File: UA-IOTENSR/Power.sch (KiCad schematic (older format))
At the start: 29 parts, among them IC1 BQ2000TPN-B5, J2 ZX62-AB-5PA_31_, U2 AP63203WU

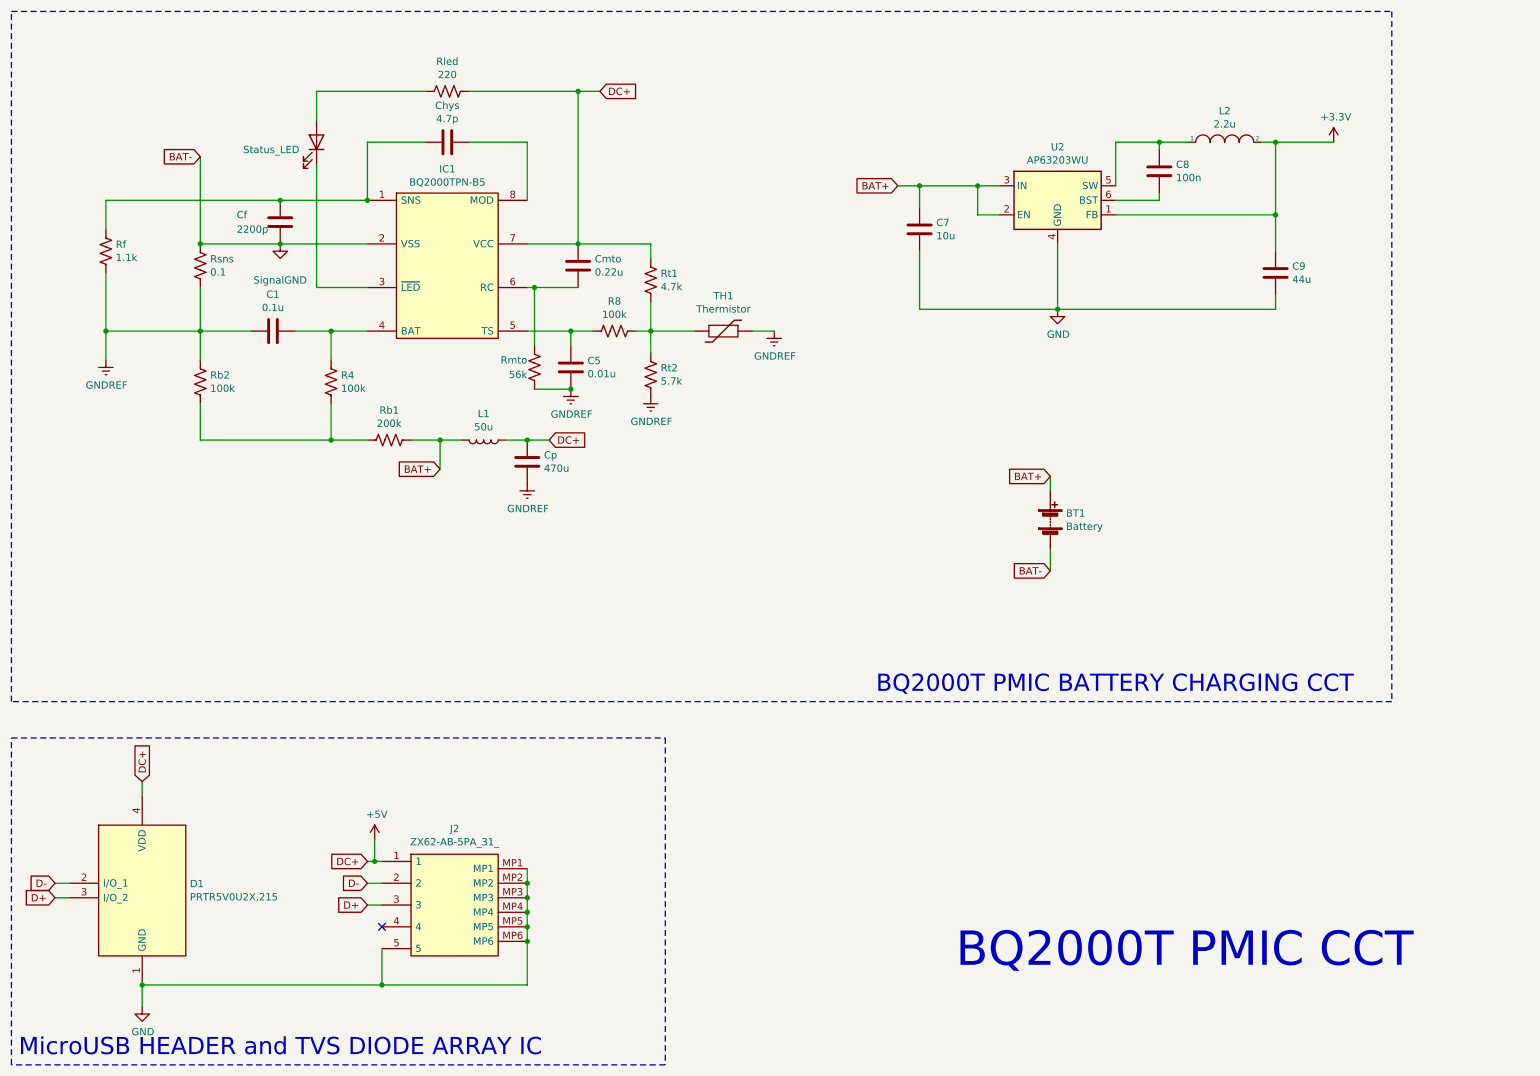
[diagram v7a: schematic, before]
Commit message: Fixed GNDs and added new capacitors
Adjusted ground connections, USB GND only connects to the Rf and the VCC by passing capacitors.
Added by pass capactitors on VCC.
Reconnected the thermistor in a pull high configuration
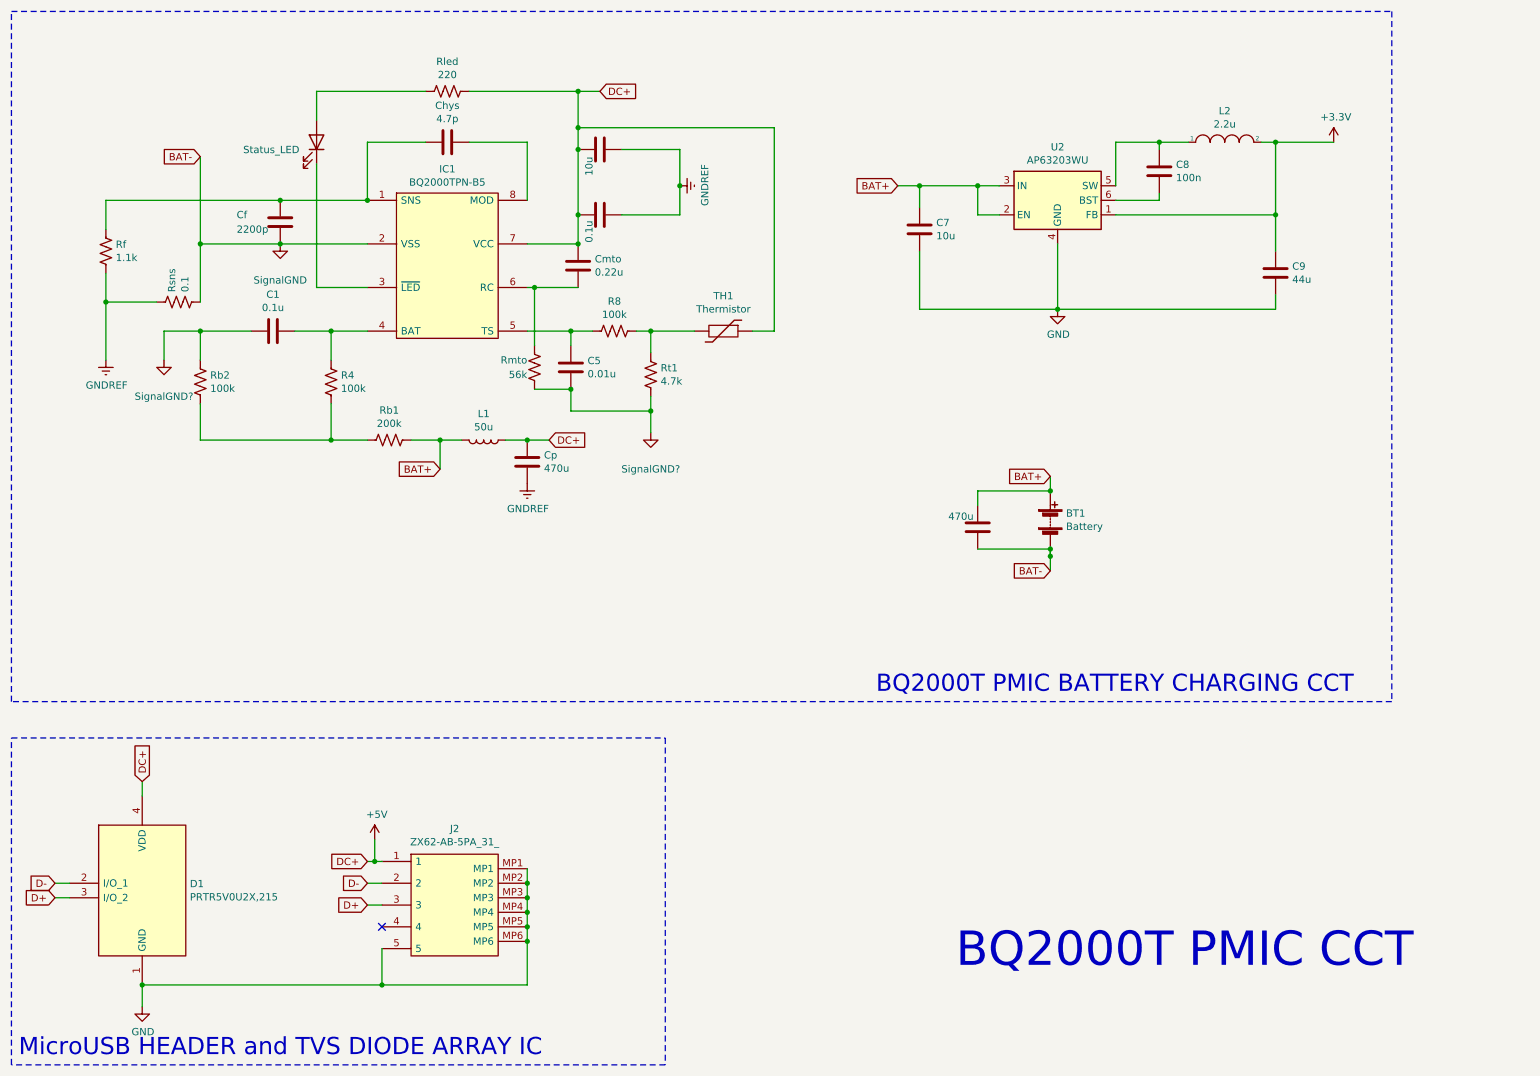
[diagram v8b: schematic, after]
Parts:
- removed Rt2: 5.7k, Resistor_SMD:R_0805_2012Metric_Pad1.20x1.40mm_HandSolder, symbol Device:R_US
- added Bypass_1: 10u, Capacitor_SMD:C_0805_2012Metric, symbol Device:C
- added Bypass_?: 0.1u, Capacitor_SMD:C_0805_2012Metric, symbol Device:C
- added Bypass_?: 470u, Capacitor_SMD:C_0805_2012Metric, symbol Device:C
- added SignalGND? (x2): GND, symbol power:GND
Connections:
- net +5V: now also TH1.1, Bypass_1.2, Bypass_?.2; no longer Rt1.1
- net BAT+: now also Bypass_?.2
- net GND: now also C1.2, C5.2, Rb2.1, Rmto.1, Rsns.2, Rt1.2, Bypass_?.1, SignalGND?.1 (GND), SignalGND?.1 (GND); no longer Rsns.1
- net GNDREF: now also Rsns.1, Bypass_1.1, Bypass_?.1; no longer C1.2, C5.2, Rb2.1, Rmto.1, Rsns.2, TH1.1
- net at R8.1, TH1.2: now also Rt1.1; no longer Rt1.2
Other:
- moved on the sheet: Rsns, Rt1
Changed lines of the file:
@@
 	0    1    1    0
 $EndComp
-Connection ~ 1150 2700
 $Comp
 L power:GNDREF #PWR07
@@
 L Device:R_US Rsns
 U 1 1 61E54493
-P 1800 2250
-F 0 "Rsns" H 1868 2296 50  0000 L CNN
-F 1 "0.1" H 1868 2205 50  0000 L CNN
-F 2 "SamacSys_Parts:RESC6331X80N" V 1840 2240 50  0001 C CNN
-F 3 "~" H 1800 2250 50  0001 C CNN
-	1    1800 2250
-	1    0    0    -1
-$EndComp
-Connection ~ 1800 2100
+P 1650 2500
+F 0 "Rsns" H 1718 2546 50  0000 L CNN
+F 1 "0.1" H 1718 2455 50  0000 L CNN
+F 2 "SamacSys_Parts:RESC6331X80N" V 1690 2490 50  0001 C CNN
+F 3 "~" H 1650 2500 50  0001 C CNN
+	1    1650 2500
+	0    -1   -1   0
+$EndComp
 $Comp
 L Device:C Cf
@@
 	1    0    0    -1
 $EndComp
-Wire Wire Line
-	1150 2700 1150 2900
 $Comp
 L Device:R_US Rb2
@@
 	3650 1050 4400 1050
 Wire Wire Line
-	4400 1050 4400 2100
-Wire Wire Line
 	3250 3450 3450 3450
 $Comp
@@
 Connection ~ 4900 2700
 $Comp
-L power:GNDREF #PWR013
-U 1 1 61E7A638
-P 4900 3150
-F 0 "#PWR013" H 4900 2900 50  0001 C CNN
-F 1 "GNDREF" H 4905 2977 50  0000 C CNN
-F 2 "" H 4900 3150 50  0001 C CNN
-F 3 "" H 4900 3150 50  0001 C CNN
-	1    4900 3150
-	1    0    0    -1
-$EndComp
-$Comp
 L Device:Thermistor TH1
 U 1 1 61E7B984
@@
 Wire Wire Line
 	4900 2700 5200 2700
-$Comp
-L power:GNDREF #PWR014
-U 1 1 61E7DEA9
-P 5750 2700
-F 0 "#PWR014" H 5750 2450 50  0001 C CNN
-F 1 "GNDREF" H 5755 2527 50  0000 C CNN
-F 2 "" H 5750 2700 50  0001 C CNN
-F 3 "" H 5750 2700 50  0001 C CNN
-	1    5750 2700
-	1    0    0    -1
-$EndComp
 Text GLabel 4200 3450 2    50   Input ~ 0
 DC+
@@
 Wire Wire Line
 	4350 3100 4100 3100
-$Comp
-L power:GNDREF #PWR012
-U 1 1 61E8BC9F
-P 4350 3100
-F 0 "#PWR012" H 4350 2850 50  0001 C CNN
-F 1 "GNDREF" H 4355 2927 50  0000 C CNN
-F 2 "" H 4350 3100 50  0001 C CNN
-F 3 "" H 4350 3100 50  0001 C CNN
-	1    4350 3100
-	1    0    0    -1
-$EndComp
-Connection ~ 4350 3100
 Wire Wire Line
 	4050 1800 4050 1400
@@
 	2950 1400 3350 1400
 Wire Wire Line
-	1150 2300 1150 2700
-Wire Wire Line
-	1800 2700 1150 2700
-Wire Wire Line
 	2150 2700 1800 2700
-Connection ~ 1800 2700
 Wire Wire Line
 	1800 2700 1800 2900
-Wire Wire Line
-	1800 2400 1800 2700
 Wire Wire Line
 	4050 2400 4100 2400
@@
 DC+
 NoConn ~ 3050 6800
-Wire Wire Line
-	4900 2100 4400 2100
-Wire Wire Line
-	4900 2200 4900 2100
-$Comp
-L Device:R_US Rt2
-U 1 1 6209F5C7
+$Comp
+L Device:R_US Rt1
+U 1 1 620A85C3
 P 4900 3000
-F 0 "Rt2" H 4968 3046 50  0000 L CNN
-F 1 "5.7k" H 4968 2955 50  0000 L CNN
+F 0 "Rt1" H 4968 3046 50  0000 L CNN
+F 1 "4.7k" H 4968 2955 50  0000 L CNN
 F 2 "Resistor_SMD:R_0805_2012Metric_Pad1.20x1.40mm_HandSolder" V 4940 2990 50  0001 C CNN
 F 3 "~" H 4900 3000 50  0001 C CNN
@@
 	1    0    0    -1
 $EndComp
-$Comp
-L Device:R_US Rt1
-U 1 1 620A85C3
-P 4900 2350
-F 0 "Rt1" H 4968 2396 50  0000 L CNN
-F 1 "4.7k" H 4968 2305 50  0000 L CNN
-F 2 "Resistor_SMD:R_0805_2012Metric_Pad1.20x1.40mm_HandSolder" V 4940 2340 50  0001 C CNN
-F 3 "~" H 4900 2350 50  0001 C CNN
-	1    4900 2350
-	1    0    0    -1
-$EndComp
-Wire Wire Line
-	4900 2500 4900 2700
 $Comp
 L Regulator_Switching:AP63203WU U2
@@
 	7650 3800 7650 3700
 Wire Wire Line
-	7650 4200 7650 4350
+	7650 4200 7650 4250
 Text GLabel 7650 3700 0    50   Input ~ 0
 BAT+
 Text GLabel 7650 4350 0    50   Input ~ 0
 BAT-
+Wire Wire Line
+	1150 2300 1150 2500
+Connection ~ 1150 2500
+Wire Wire Line
+	1150 2500 1150 2900
+Wire Wire Line
+	1800 2500 1800 2100
+Connection ~ 1800 2100
+Wire Wire Line
+	1150 2500 1500 2500
+$Comp
+L power:GND SignalGND?
+U 1 1 624B40F1
+P 1550 2900
+F 0 "SignalGND?" H 1550 2650 50  0000 C CNN
+F 1 "GND" H 1555 2727 50  0001 C CNN
+F 2 "" H 1550 2900 50  0001 C CNN
+F 3 "" H 1550 2900 50  0001 C CNN
+	1    1550 2900
+	1    0    0    -1
+$EndComp
+Connection ~ 1800 2700
+Wire Wire Line
+	1550 2700 1800 2700
+Wire Wire Line
+	1550 2700 1550 2900
+Wire Wire Line
+	5750 2700 5750 1300
+Wire Wire Line
+	5750 1300 4400 1300
+Wire Wire Line
+	4400 1050 4400 1300
+Connection ~ 4400 1300
+Wire Wire Line
+	4400 1300 4400 1450
+$Comp
+L power:GND SignalGND?
+U 1 1 624C105D
+P 4900 3400
+F 0 "SignalGND?" H 4900 3150 50  0000 C CNN
+F 1 "GND" H 4905 3227 50  0001 C CNN
+F 2 "" H 4900 3400 50  0001 C CNN
+F 3 "" H 4900 3400 50  0001 C CNN
+	1    4900 3400
+	1    0    0    -1
+$EndComp
+Wire Wire Line
+	4350 3100 4350 3250
+Wire Wire Line
+	4350 3250 4900 3250
+Wire Wire Line
+	4900 3150 4900 3250
+Connection ~ 4350 3100
+Connection ~ 4900 3250
+Wire Wire Line
+	4900 3250 4900 3400
+$Comp
+L Device:C Bypass_1
+U 1 1 624CCAA1
+P 4550 1450
+F 0 "Bypass_1" H 4665 1496 50  0001 C BNN
+F 1 "10u" H 4665 1405 50  0000 C TNN
+F 2 "Capacitor_SMD:C_0805_2012Metric" H 4588 1300 50  0001 C CNN
+F 3 "~" H 4550 1450 50  0001 C CNN
+	1    4550 1450
+	0    1    1    0
+$EndComp
+Connection ~ 4400 1450
+Wire Wire Line
+	4400 1450 4400 1900
+$Comp
+L Device:C Bypass_?
+U 1 1 624D22AD
+P 4550 1900
+F 0 "Bypass_?" H 4665 1946 50  0001 C BNN
+F 1 "0.1u" H 4665 1855 50  0000 C TNN
+F 2 "Capacitor_SMD:C_0805_2012Metric" H 4588 1750 50  0001 C CNN
+F 3 "~" H 4550 1900 50  0001 C CNN
+	1    4550 1900
+	0    1    1    0
+$EndComp
+Connection ~ 4400 1900
+Wire Wire Line
+	4400 1900 4400 2100
+$Comp
+L power:GNDREF #PWR?
+U 1 1 624D3CDF
+P 5100 1700
+F 0 "#PWR?" H 5100 1450 50  0001 C CNN
+F 1 "GNDREF" H 5105 1527 50  0000 C CNN
+F 2 "" H 5100 1700 50  0001 C CNN
+F 3 "" H 5100 1700 50  0001 C CNN
+	1    5100 1700
+	0    -1   -1   0
+$EndComp
+Wire Wire Line
+	4700 1450 5100 1450
+Wire Wire Line
+	5100 1450 5100 1700
+Wire Wire Line
+	5100 1900 4700 1900
+Connection ~ 5100 1700
+Wire Wire Line
+	5100 1700 5100 1900
+$Comp
+L Device:C Bypass_?
+U 1 1 624D9D33
+P 7150 4050
+F 0 "Bypass_?" H 7265 4096 50  0001 C BNN
+F 1 "470u" H 7265 4005 50  0000 C TNN
+F 2 "Capacitor_SMD:C_0805_2012Metric" H 7188 3900 50  0001 C CNN
+F 3 "~" H 7150 4050 50  0001 C CNN
+	1    7150 4050
+	-1   0    0    1
+$EndComp
+Wire Wire Line
+	7150 3800 7650 3800
+Wire Wire Line
+	7150 3800 7150 3900
+Connection ~ 7650 3800
+Wire Wire Line
+	7150 4200 7650 4200
+Wire Wire Line
+	7650 4200 7650 4250
+Connection ~ 7650 4200
+Connection ~ 7650 4250
+Wire Wire Line
+	7650 4250 7650 4350
 $EndSCHEMATC
